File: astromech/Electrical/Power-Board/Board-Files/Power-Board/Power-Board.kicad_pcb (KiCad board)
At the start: 2 copper layers, 119.4 x 96.5 mm, 79 parts, among them J1 BAT_IN_SCREW, J10 HEAD_MOT, J2 BAT_IN_HOLE, J5 E_STOP, J6 CTRL_BRD, J7 JETSON, J8 L_DRIVE, J9 R_DRIVE, Q1 Q_NMOS_DSG, Q2 Q_NMOS_DSG, U1 LTC7003, U2 Logic_Level_Converter, U3 12V_REG, U4 LTC7003, U5 5V_REG, U6 3.3V_REG

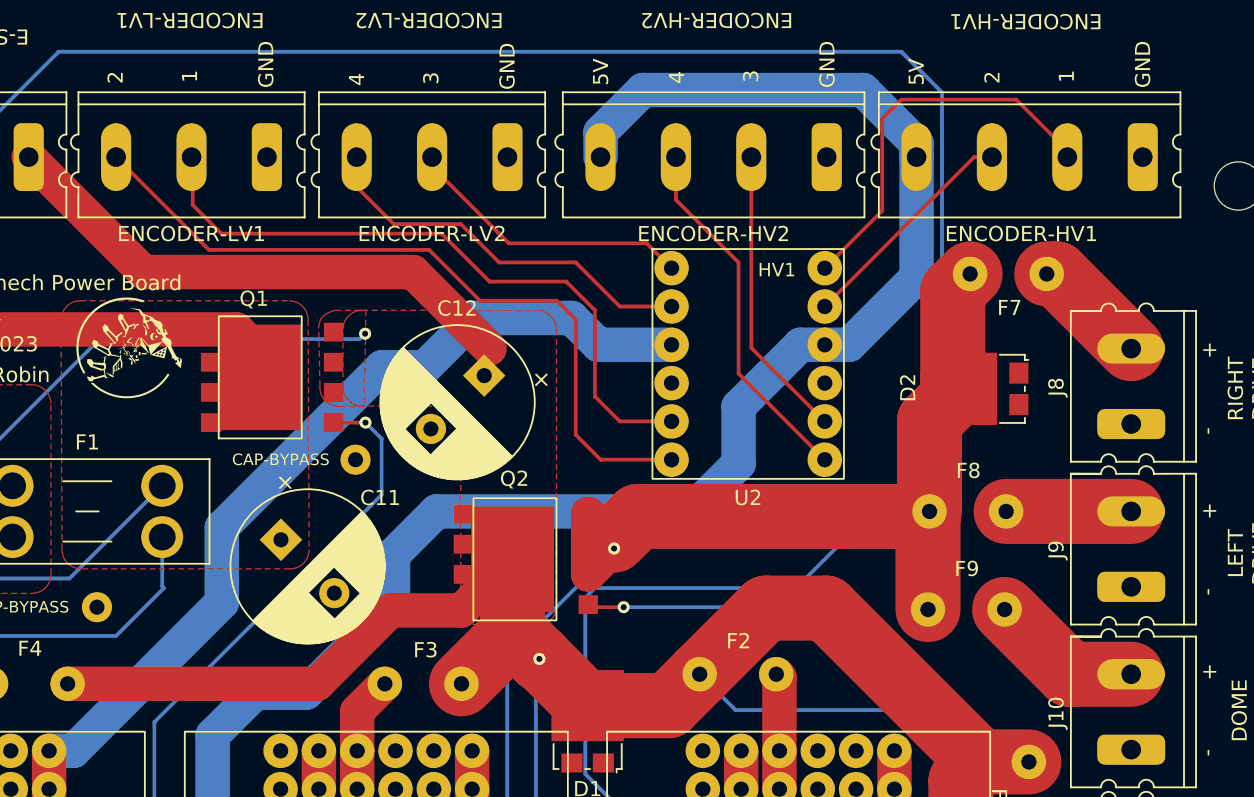
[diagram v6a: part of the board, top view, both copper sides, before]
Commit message: changed fuse spacing
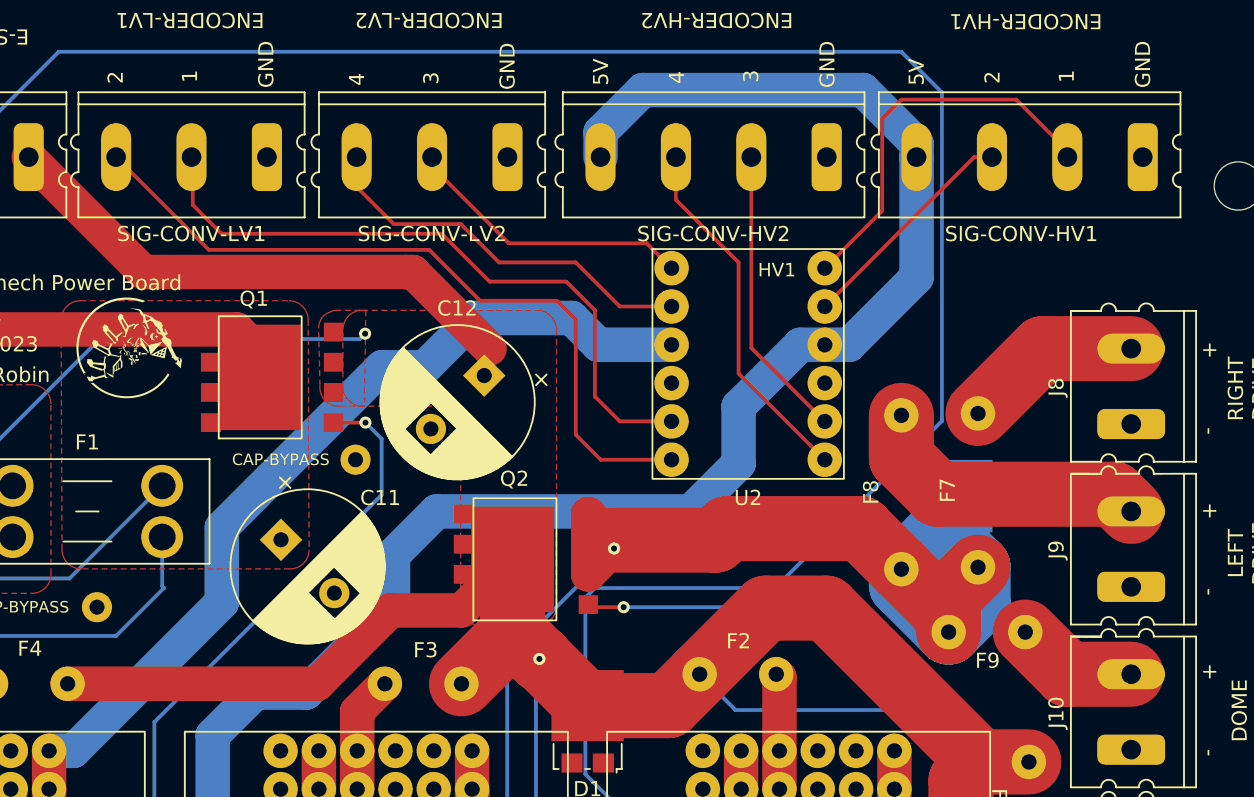
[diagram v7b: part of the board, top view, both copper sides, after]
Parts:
- D2: moved to B.Cu
- F7, F8: footprint astromech-footprints:Generic-Fuse -> astromech-footprints:10.2mm fuse
- moved F7 14.5 mm to (174.6, 71.0), turned to 90 degrees
- moved D2 7.12 mm to (174.3, 71.4), turned to 90 degrees
- moved F8 4.62 mm to (169.5, 71.1), turned to 90 degrees
- moved F9 2.03 mm to (175.3, 80.4)
- renumbered ENCODER-HV1 to SIG-CONV-HV1, ENCODER-HV2 to SIG-CONV-HV2, ENCODER-LV1 to SIG-CONV-LV1, ENCODER-LV2 to SIG-CONV-LV2
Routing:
- net MOT_VOLTAGE: track 94.0 -> 106.2 mm
- net Net-(F8-Pad2): track 8.29 -> 19.5 mm
- net Net-(F7-Pad2): track 7.65 -> 11.9 mm
- net Net-(F9-Pad2): track 10.2 -> 8.18 mm
- net Net-(J5-Pad2): track 145.9 -> 145.0 mm
